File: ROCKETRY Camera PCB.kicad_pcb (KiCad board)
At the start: 2 copper layers, 111.8 x 67.7 mm, 29 parts, among them J1 Conn_01x03_Pin, J2 Conn_01x01_Pin, J3 Conn_01x01_Pin, J4 Conn_01x01_Pin, J5 Conn_01x02_Pin, U3 AP62200WU

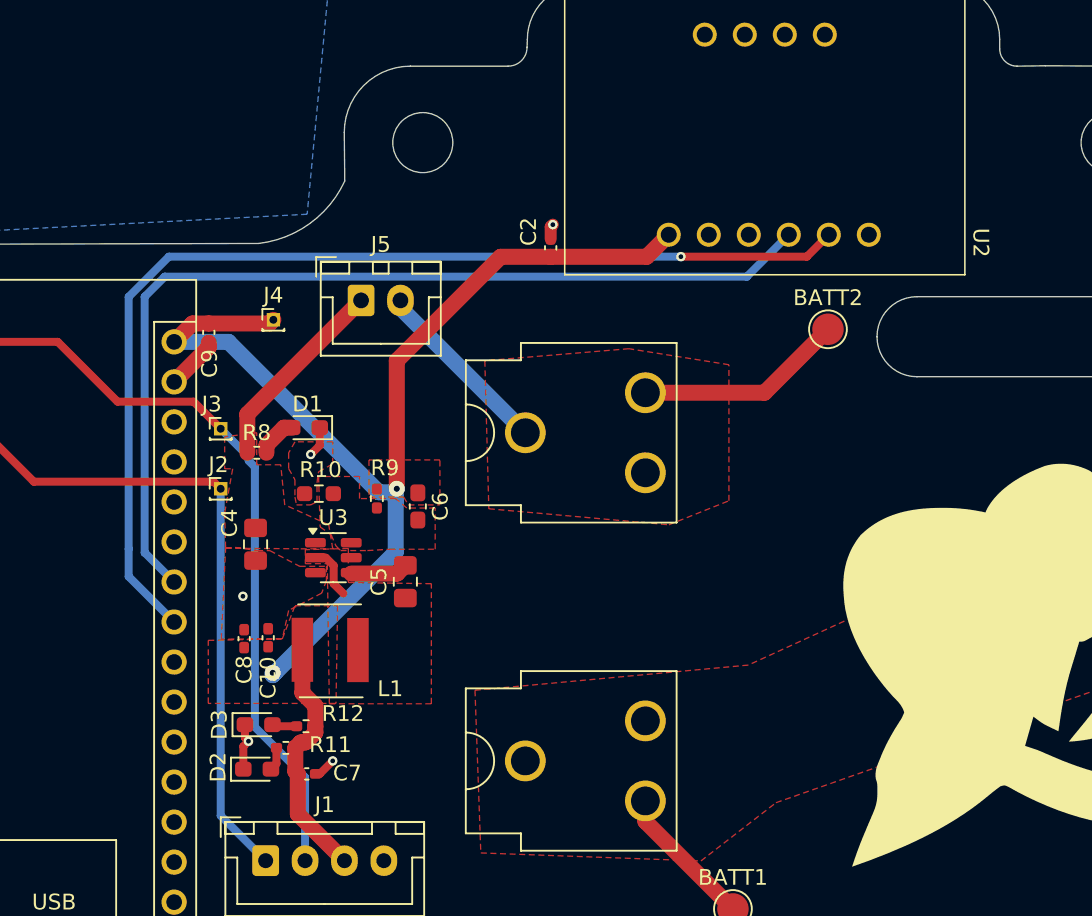
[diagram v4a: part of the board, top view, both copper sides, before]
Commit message: made critical updates based on Aila's feedback
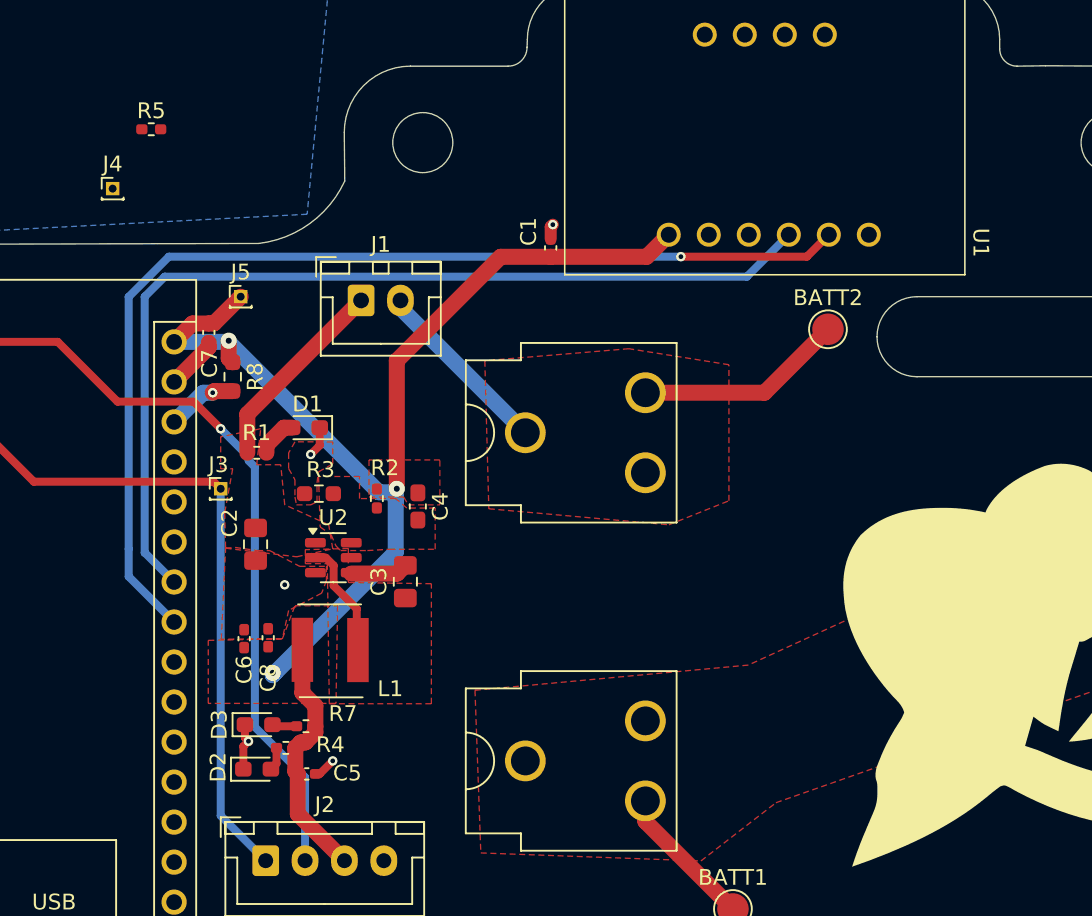
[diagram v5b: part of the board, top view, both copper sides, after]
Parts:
- removed the J3 at (105.2, 86.6)
- added J4: Conn_01x01_Pin, Connector_PinHeader_1.00mm:PinHeader_1x01_P1.00mm_Vertical, F.Cu at (98.3, 71.4)
- added R5: 0, Resistor_SMD:R_0402_1005Metric_Pad0.72x0.64mm_HandSolder, F.Cu at (100.7, 67.6)
- added R8: 10k, Resistor_SMD:R_0603_1608Metric_Pad0.98x0.95mm_HandSolder, F.Cu at (105.9, 83.3)
- moved J5 2.54 mm to (106.4, 78.2)
- renumbered C2 to C1, C4 to C2, C5 to C3, C6 to C4, C7 to C5, C8 to C6, C9 to C7, C10 to C8, J5 to J1, J1 to J2, J2 to J3, J4 to J5, R8 to R1, R9 to R2, R10 to R3, R11 to R4, R12 to R7, U2 to U1, U3 to U2
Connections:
- A1 pad 27: unconnected-(A1-+5V-Pad27) -> Net-(A1-+5V)
- A1 pad 28: unconnected-(A1-~{RESET}-Pad28) -> Net-(A1-~{RESET}-Pad28)
- A1 pad 3: unconnected-(A1-~{RESET}-Pad3) -> Net-(A1-~{RESET}-Pad28)
- C5 pad 1: +5V -> Net-(J2-Pin_3)
- D2 pad 1: GND -> Net-(D2-K)
- J2 pad 3: +5V -> Net-(J2-Pin_3)
- R4 pad 1: +5V -> Net-(J2-Pin_3)
- U1 pad 2: unconnected-(U2-I2-Pad2) -> GND
- U1 pad 3: unconnected-(U2-SNO-Pad3) -> GND
- U1 pad 4: unconnected-(U2-CS-Pad4) -> GND
- U1 pad 9: unconnected-(U2-INT-Pad9) -> GND
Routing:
- net Net-(A1-~{RESET}-Pad28): track 0.00 -> 4.53 mm, vias 0 -> 1
- net Net-(U2-SW): track 3.40 -> 7.37 mm
- net +5V: vias 2 -> 3
- net Net-(A1-D1/TX): vias 0 -> 1

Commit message: finished with updates, has my approval to order
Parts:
- removed J3: Conn_01x01_Pin, Connector_PinHeader_1.00mm:PinHeader_1x01_P1.00mm_Vertical
- J4: footprint Connector_PinHeader_1.00mm:PinHeader_1x01_P1.00mm_Vertical -> custom:mouonting_hole
- moved R5 41.4 mm to (113.0, 107.1), turned to -90 degrees
- moved J4 22.0 mm to (104.5, 92.5)
- moved C5 3.44 mm to (113.5, 110.4)
- moved R4 1.31 mm to (110.6, 106.8)
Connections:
- A1 pad 10: unconnected-(A1-D7-Pad10) -> GND
- A1 pad 11: unconnected-(A1-D8-Pad11) -> GND
- A1 pad 12: unconnected-(A1-D9-Pad12) -> GND
- A1 pad 13: unconnected-(A1-D10-Pad13) -> GND
- A1 pad 14: unconnected-(A1-D11-Pad14) -> GND
- A1 pad 15: unconnected-(A1-D12-Pad15) -> GND
- A1 pad 16: unconnected-(A1-D13-Pad16) -> GND
- A1 pad 18: unconnected-(A1-AREF-Pad18) -> GND
- A1 pad 19: unconnected-(A1-A0-Pad19) -> GND
- A1 pad 20: unconnected-(A1-A1-Pad20) -> GND
- A1 pad 21: unconnected-(A1-A2-Pad21) -> GND
- A1 pad 22: unconnected-(A1-A3-Pad22) -> GND
- A1 pad 25: unconnected-(A1-A6-Pad25) -> GND
- A1 pad 26: unconnected-(A1-A7-Pad26) -> GND
- A1 pad 5: unconnected-(A1-D2-Pad5) -> GND
- A1 pad 6: unconnected-(A1-D3-Pad6) -> GND
- A1 pad 7: unconnected-(A1-D4-Pad7) -> GND
- A1 pad 8: unconnected-(A1-D5-Pad8) -> GND
- A1 pad 9: unconnected-(A1-D6-Pad9) -> GND
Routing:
- net Net-(A1-~{RESET}-Pad28): track 4.53 -> 19.8 mm, vias 1 -> 2
- net GND: track 10.9 -> 24.7 mm, vias 5 -> 4
- net Net-(J2-Pin_3): track 0.00 -> 8.56 mm
- net +5V: track 85.2 -> 76.9 mm
- net Net-(A1-+5V): track 0.00 -> 6.15 mm
- net Net-(D2-A): track 1.50 -> 2.25 mm

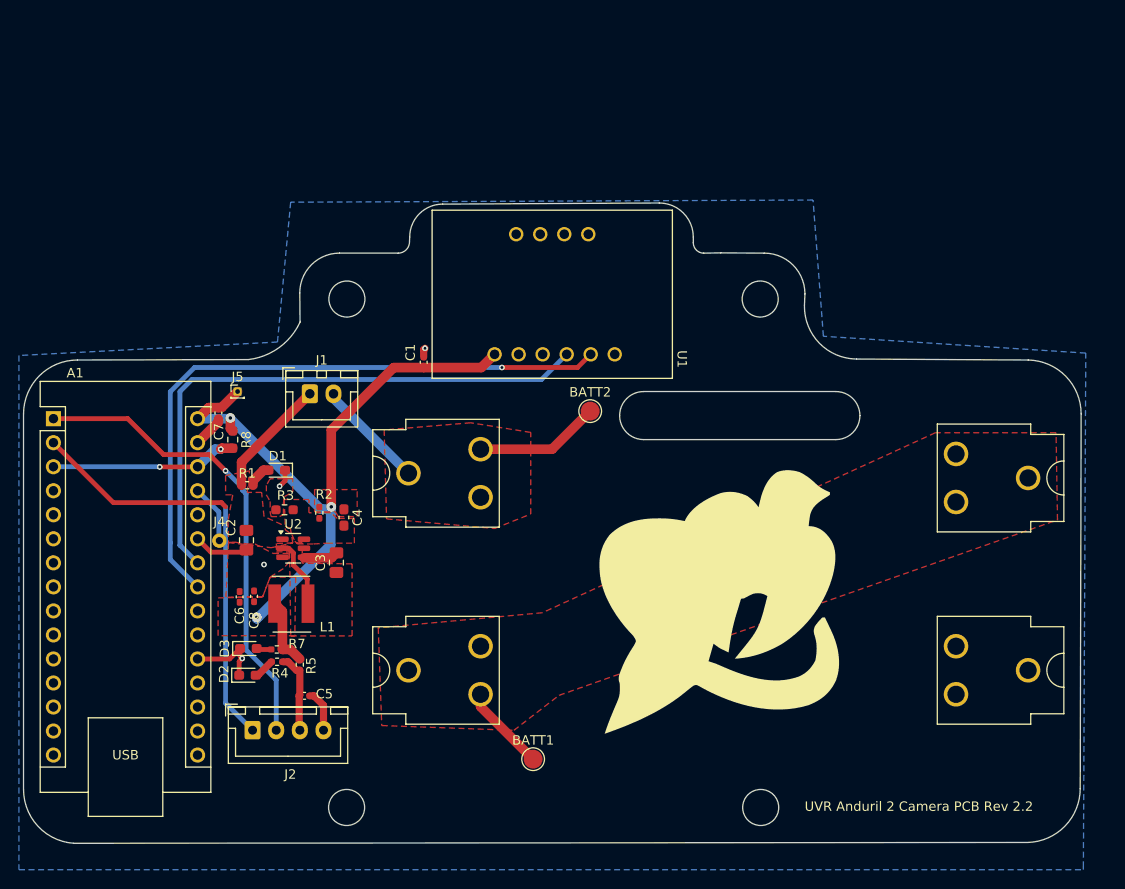
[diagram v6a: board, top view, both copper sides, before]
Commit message: the board was a bit deformed. it should be better now
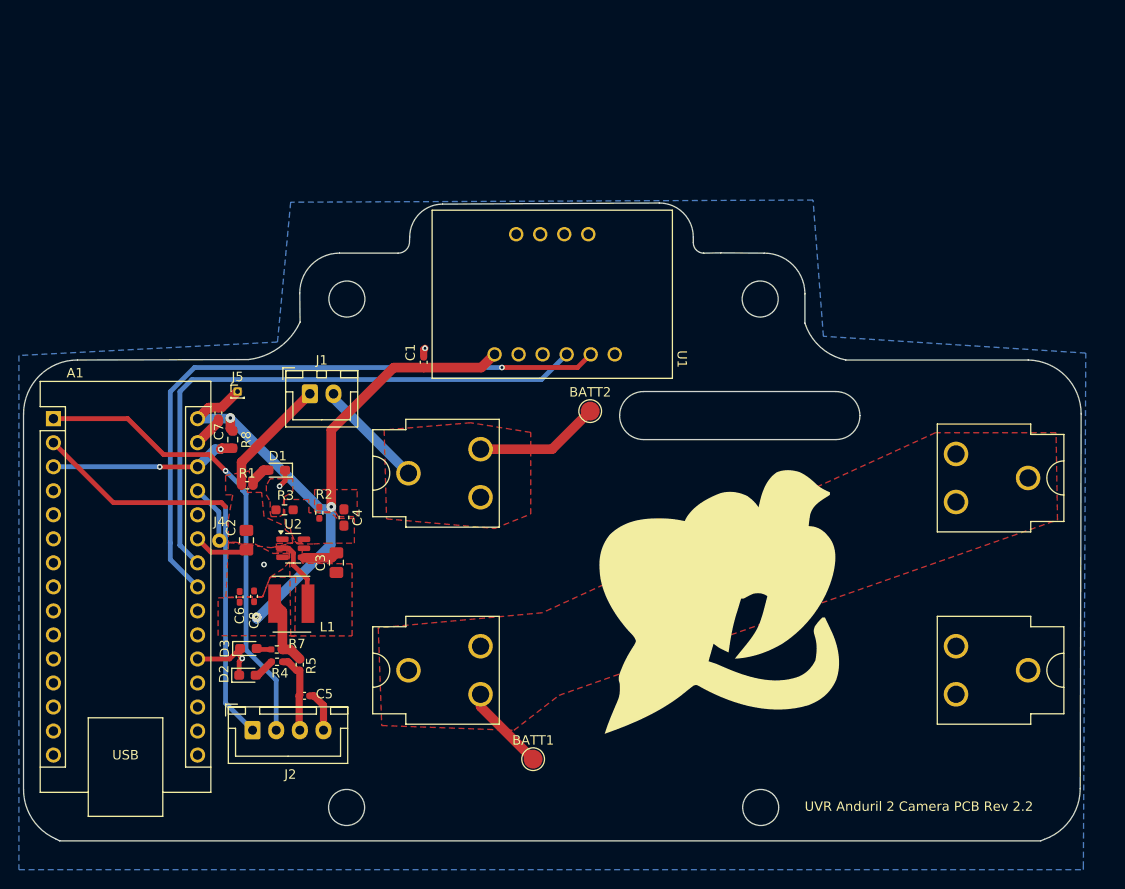
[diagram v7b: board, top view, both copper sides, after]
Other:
- board size 111.8 x 67.7 mm -> 111.8 x 67.4 mm
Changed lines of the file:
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@@
 			)
 			(height 0)
-			(gr_text "69.0000 mm"
+			(gr_text "2716.5354 mils"
 				(at 157.492 114.546 0)
 				(layer "User.1")
@@
 			)
 			(height 0)
-			(gr_text "69.0000 mm"
+			(gr_text "2716.5354 mils"
 				(at 156.992 93.973 0)
 				(layer "User.1")
@@
 	)
 	(gr_line
+		(start 87.63 125.73)
+		(end 87.18594 125.509139)
+		(stroke
+			(width 0.05)
+			(type default)
+		)
+		(layer "Edge.Cuts")
+	)
+	(gr_line
 		(start 124.6 62.4)
 		(end 124.62 61.9)
@@
 		(layer "Edge.Cuts")
 	)
+	(gr_line
+		(start 191.712811 125.569465)
+		(end 191.32 125.73)
+		(stroke
+			(width 0.05)
+			(type default)
+		)
+		(layer "Edge.Cuts")
+	)
 	(gr_arc
 		(start 124.6 62.4)
@@
 	)
 	(gr_arc
-		(start 171.857121 74.797707)
-		(mid 167.932373 73.125641)
-		(end 166.3492 69.1642)
+		(start 170.72 74.899999)
+		(mid 168.033704 73.534835)
+		(end 166.39897 71.003531)
 		(stroke
 			(width 0.05)
@@
 	)
 	(gr_line
-		(start 166.3492 69.1642)
+		(start 166.4 71)
 		(end 166.4 67.9)
 		(stroke
@@
 	(gr_arc
 		(start 195.5 120.2)
-		(mid 193.900567 124.159211)
-		(end 189.999877 125.896494)
+		(mid 194.457951 123.485345)
+		(end 191.712811 125.569465)
 		(stroke
 			(width 0.05)
@@
 		(layer "Edge.Cuts")
 	)
+	(gr_line
+		(start 87.63 125.73)
+		(end 191.32 125.73)
+		(stroke
+			(width 0.05)
+			(type default)
+		)
+		(layer "Edge.Cuts")
+	)
 	(gr_circle
 		(center 161.725 122.2)
@@
 	(gr_line
 		(start 190 74.900001)
-		(end 171.857121 74.797707)
+		(end 170.72 74.9)
 		(stroke
 			(width 0.05)
@@
 	)
 	(gr_arc
-		(start 89.100981 125.986017)
-		(mid 85.330803 124.186875)
+		(start 87.18594 125.509139)
+		(mid 84.720871 123.406434)
 		(end 83.8 120.3)
 		(stroke
@@
 		(layer "Edge.Cuts")
 	)
-	(gr_line
-		(start 189.999877 125.896494)
-		(end 89.100981 125.986017)
-		(stroke
-			(width 0.05)
-			(type default)
-		)
-		(layer "Edge.Cuts")
-	)
 	(gr_arc
 		(start 155.7 63.6)
@@
 		)
 		(height 2.57)
-		(gr_text "29.2000 mm"
+		(gr_text "1149.6063 mils"
 			(at 181.102 76.454 0)
 			(layer "User.4")
@@
 		)
 		(height 10.394)
-		(gr_text "53.4000 mm"
+		(gr_text "2102.3622 mils"
 			(at 72.256 101.6 90)
 			(layer "User.4")
@@
 		)
 		(height 2.255999)
-		(gr_text "29.9000 mm"
+		(gr_text "1177.1654 mils"
 			(at 109.594001 59.95 90)
 			(layer "User.4")
@@
 		)
 		(height 2.569999)
-		(gr_text "29.2000 mm"
+		(gr_text "1149.6063 mils"
 			(at 98.4 76.319999 0)
 			(layer "User.4")
@@
 		)
 		(height -10.167919)
-		(gr_text "53.4001 mm"
+		(gr_text "2102.3659 mils"
 			(at 139.678805 33.632101 0.1072953418)
 			(layer "User.4")
@@
 		)
 		(height 3.802362)
-		(gr_text "51.1812 mm"
+		(gr_text "2015.0062 mils"
 			(at 115.521146 73.857081 270.1421729)
 			(layer "User.5")
@@
 		)
 		(height 5.334)
-		(gr_text "43.1800 mm"
+		(gr_text "1700.0000 mils"
 			(at 139.7 52.444 0)
 			(layer "User.5")
@@
 		)
 		(height 3.254887)
-		(gr_text "55.4991 mm"
+		(gr_text "2185.0057 mils"
 			(at 114.554 127.254 89.86888861)
 			(layer "User.5")
@@
 		)
 		(height 22.098)
-		(gr_text "38.7350 mm"
+		(gr_text "1525.0000 mils"
 			(locked yes)
 			(at 139.3825 160.648 0)

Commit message: final touches before exporting gerbers
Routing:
- net Net-(A1-D0/RX): vias 0 -> 1
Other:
- outline, holes or cut-outs redrawn
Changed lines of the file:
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@@
 	)
 	(gr_arc
-		(start 170.72 74.899999)
-		(mid 168.033704 73.534835)
-		(end 166.39897 71.003531)
+		(start 170.729058 74.856774)
+		(mid 168.024537 73.466779)
+		(end 166.41 70.89)
 		(stroke
 			(width 0.05)
@@
 	)
 	(gr_line
-		(start 166.4 71)
+		(start 166.41 70.89)
 		(end 166.4 67.9)
 		(stroke
@@
 	)
 	(gr_line
-		(start 107.569 74.8538)
+		(start 107.09 74.93)
 		(end 89.5 74.9)
 		(stroke
@@
 	)
 	(gr_line
+		(start 170.729058 74.856774)
+		(end 171.1 74.93)
+		(stroke
+			(width 0.05)
+			(type default)
+		)
+		(layer "Edge.Cuts")
+	)
+	(gr_line
 		(start 157.5054 63.5762)
 		(end 162.1 63.6)
@@
 	)
 	(gr_arc
-		(start 113.03 70.8914)
-		(mid 110.816978 73.585791)
-		(end 107.569 74.8538)
+		(start 113.030051 70.891423)
+		(mid 110.817 73.585808)
+		(end 107.569 74.853799)
 		(stroke
 			(width 0.05)
@@
 	(gr_line
 		(start 190 74.900001)
-		(end 170.72 74.9)
+		(end 171.1 74.93)
+		(stroke
+			(width 0.05)
+			(type default)
+		)
+		(layer "Edge.Cuts")
+	)
+	(gr_line
+		(start 107.569 74.8538)
+		(end 107.09 74.93)
 		(stroke
 			(width 0.05)
@@
 		(net 3)
 	)
+	(via
+		(at 105.156 90.424)
+		(size 0.6)
+		(drill 0.3)
+		(layers "F.Cu" "B.Cu")
+		(net 3)
+	)
